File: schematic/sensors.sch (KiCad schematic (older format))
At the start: 29 parts, among them J10 Conn_01x03, J11 Conn_01x03, J6 Conn_01x03, J7 Conn_01x02, J8 Conn_01x03_Female, J9 Conn_01x03, U3 ADS1015IDGS, U4 FAN4860UC5X, U5 LIS2MDL, U6 LSM6DSOX, U7 BME280

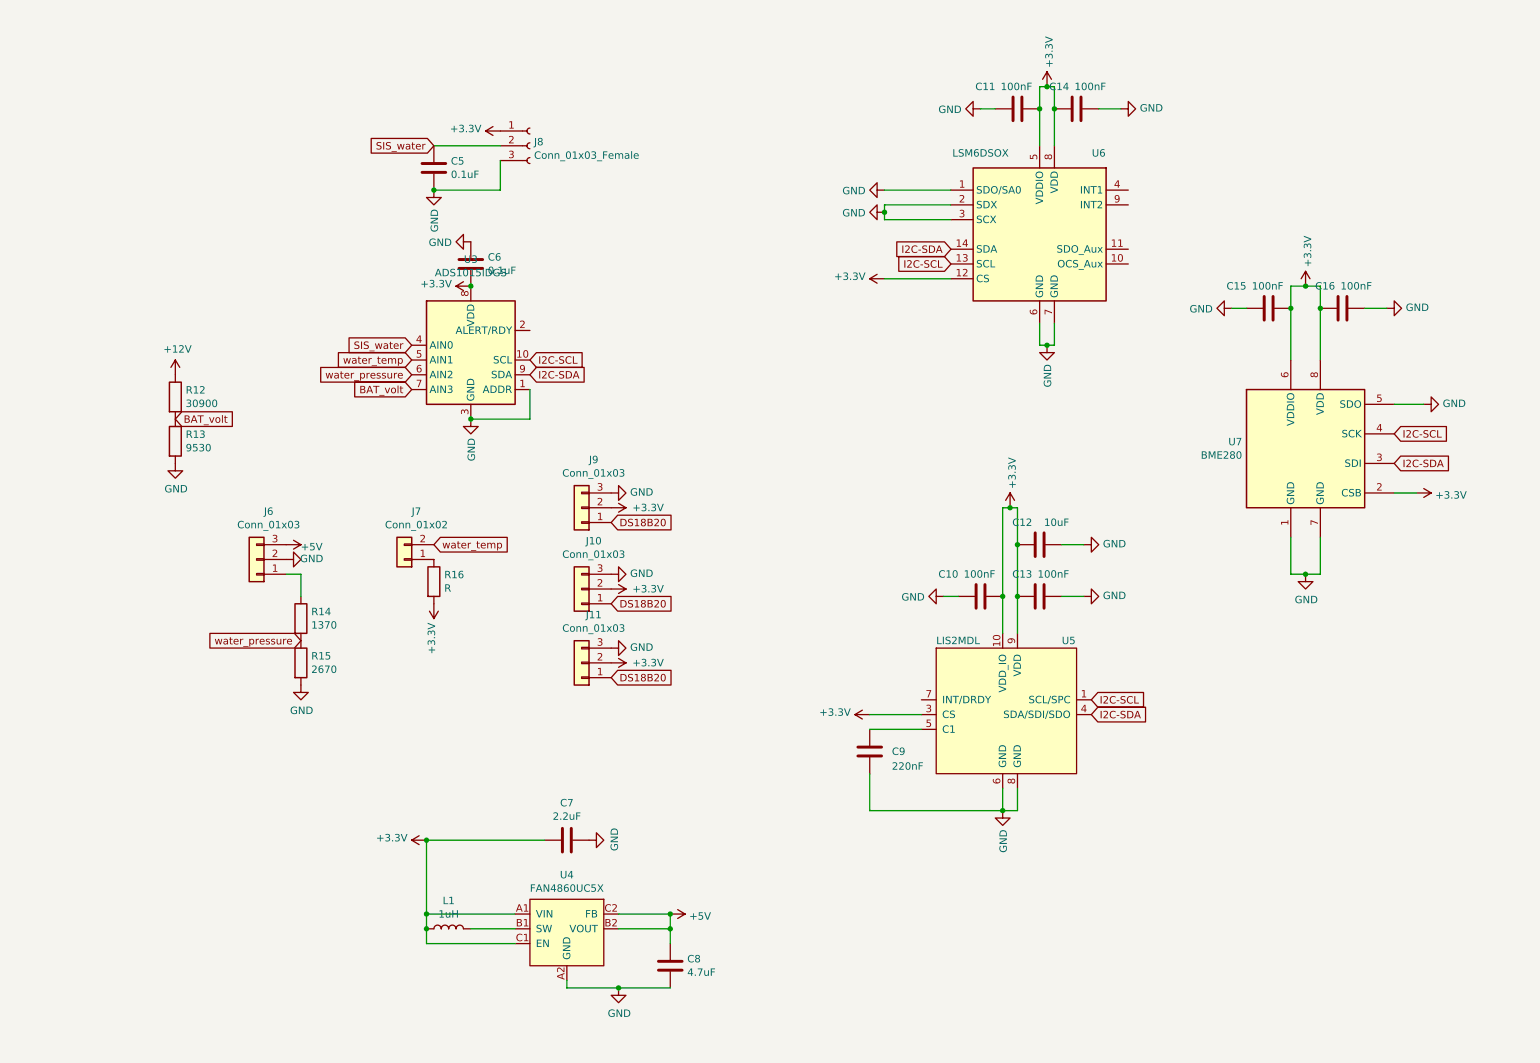
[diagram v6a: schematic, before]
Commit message: added MAX6682 for termistor
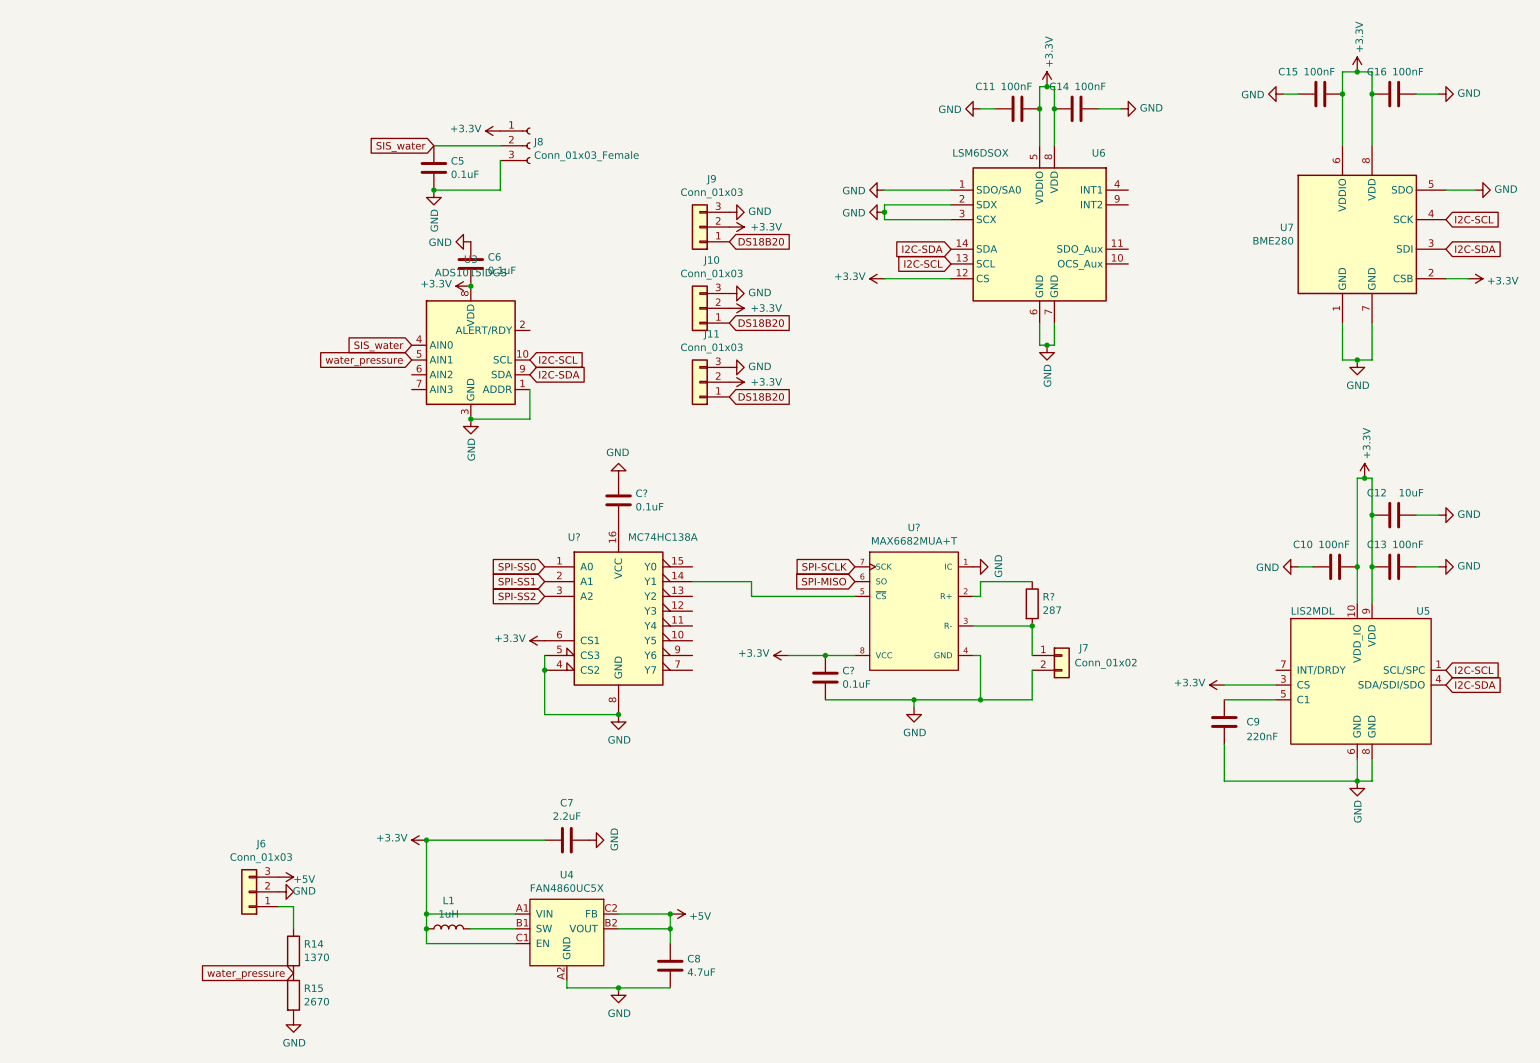
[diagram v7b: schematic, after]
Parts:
- removed R12: 30900, Resistor_SMD:R_0805_2012Metric_Pad1.15x1.40mm_HandSolder, symbol Device:R
- removed R13: 9530, Resistor_SMD:R_0805_2012Metric_Pad1.15x1.40mm_HandSolder, symbol Device:R
- removed R16: R, Resistor_SMD:R_0805_2012Metric_Pad1.15x1.40mm_HandSolder, symbol Device:R
- added C? (x2): 0.1uF, Capacitor_SMD:C_0805_2012Metric_Pad1.15x1.40mm_HandSolder, symbol Device:C
- added R?: 287, Resistor_SMD:R_0805_2012Metric_Pad1.15x1.40mm_HandSolder, symbol Device:R
- added U?: MAX6682MUA+T, Maxim-MAX6682MUA+T-*, symbol eec:MAX6682MUA+T
- added U?: MC74HC138A, symbol Apsu_Library:MC74HC138A
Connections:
- net +3V3: now also C?.1, U?.6 (CS1), U?.8 (VCC)
- net GND: now also J7.2 (Pin_2), C?.1, C?.2, U?.1 (IC), U?.4 (CS2), U?.4 (GND), U?.5 (CS3), U?.8 (GND)
- net water_pressure: now also U3.5 (AIN1); no longer U3.6 (AIN2)
- net at J7.1 (Pin_1): now also R?.2, U?.3 (R-)
- net BAT_volt: no longer names the net of U3.7 (AIN3)
- removed net water_temp: J7.2 (Pin_2), U3.5 (AIN1)
- new net: R?.1, U?.2 (R+)
- new net: U?.14 (Y1), U?.5 (~CS~)
- new net: C?.2, U?.16 (VCC)
- new net SPI-MISO: U?.6 (SO)
- new net SPI-SCLK: U?.7 (SCK)
- new net SPI-SS0: U?.1 (A0)
- new net SPI-SS1: U?.2 (A1)
- new net SPI-SS2: U?.3 (A2)
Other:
- moved on the sheet: C10, C12, C13, C15, C16, C9, J10, J11, J6, J7, J9, R14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

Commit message: new components on pcb
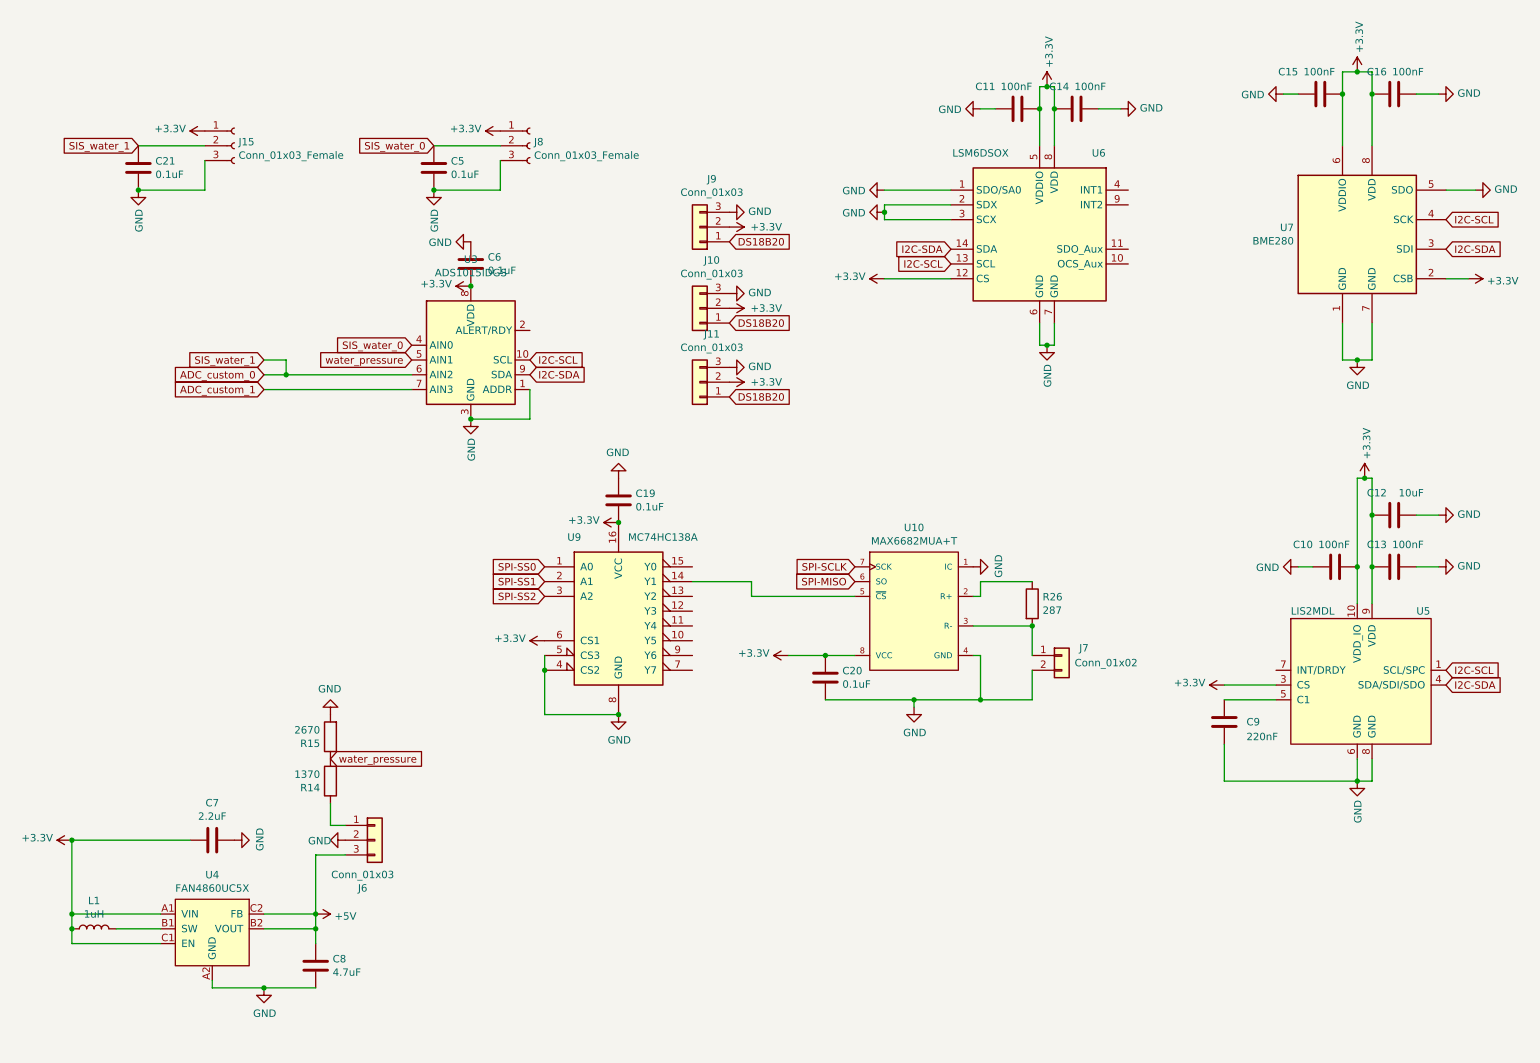
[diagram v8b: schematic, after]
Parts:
- added C21: 0.1uF, Capacitor_SMD:C_0805_2012Metric_Pad1.15x1.40mm_HandSolder, symbol Device:C
- added J15: Conn_01x03_Female, Connector_JST:JST_XH_B3B-XH-A_1x03_P2.50mm_Vertical, symbol Connector:Conn_01x03_Female
- U10: renamed from U?; footprint Maxim-MAX6682MUA+T-* -> MAX6682:Maxim-MAX6682MUA+T-Level_A
- U9: renamed from U?; footprint (none) -> Package_SO:TSSOP-16_4.4x5mm_P0.65mm
- gave numbers to parts that had none: 3
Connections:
- net +3V3: now also C19.2, U9.16 (VCC), J15.1 (Pin_1)
- net GND: now also C21.2, J15.3 (Pin_3)
- net ADC_custom_0: now reaches U3.6 (AIN2)
- net ADC_custom_0: now also C21.1, J15.2 (Pin_2)
- net ADC_custom_1: now reaches U3.7 (AIN3)
- net SIS_water renamed SIS_water_0
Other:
- moved on the sheet: C7, C8, J6, L1, R14, R15, U4
